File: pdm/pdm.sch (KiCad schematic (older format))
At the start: 27 parts, among them J1 Conn_01x05, J2 Conn_01x04_Male, U1 AZ1117CH-3_3TRG1, U2 SN65HVD233, U3 STM32F103C8Tx

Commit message: small changes
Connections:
- net _P: now reaches J2.3 (Pin_3), R2.2, U2.6 (CANL)
- net _N: now reaches J2.2 (Pin_2), R2.1, U2.7 (CANH)
- net PD0 renamed OSC_N
- net PD1 renamed OSC_P
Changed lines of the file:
@@
 EESchema Schematic File Version 4
+LIBS:pdm-cache
 EELAYER 30 0
 EELAYER END
@@
 	5050 4950 4850 4950
 Text Label 4850 4850 0    50   ~ 0
-PD0
+OSC_N
 Text Label 4850 4950 0    50   ~ 0
-PD1
+OSC_P
 $Comp
 L Device:C C9
@@
 	950  7350 1250 7350
 Text Label 2000 3850 2    50   ~ 0
-PD1
+OSC_P
 Wire Wire Line
 	1050 3850 1050 4550
 Text Label 2000 4550 2    50   ~ 0
-PD0
+OSC_N
 Wire Wire Line
 	1650 3850 2000 3850
@@
 	900  6850 1250 6850
 $Comp
-L power:+12V #PWR?
+L power:+12V #PWR0108
 U 1 1 5FA6CF0E
 P 1050 6500
-F 0 "#PWR?" H 1050 6350 50  0001 C CNN
+F 0 "#PWR0108" H 1050 6350 50  0001 C CNN
 F 1 "+12V" H 1065 6673 50  0000 C CNN
 F 2 "" H 1050 6500 50  0001 C CNN
@@
 	1    0    0    -1
 $EndComp
+Text Label 2850 2700 0    50   ~ 0
+_N
+Text Label 2850 2800 0    50   ~ 0
+_P
 $EndSCHEMATC

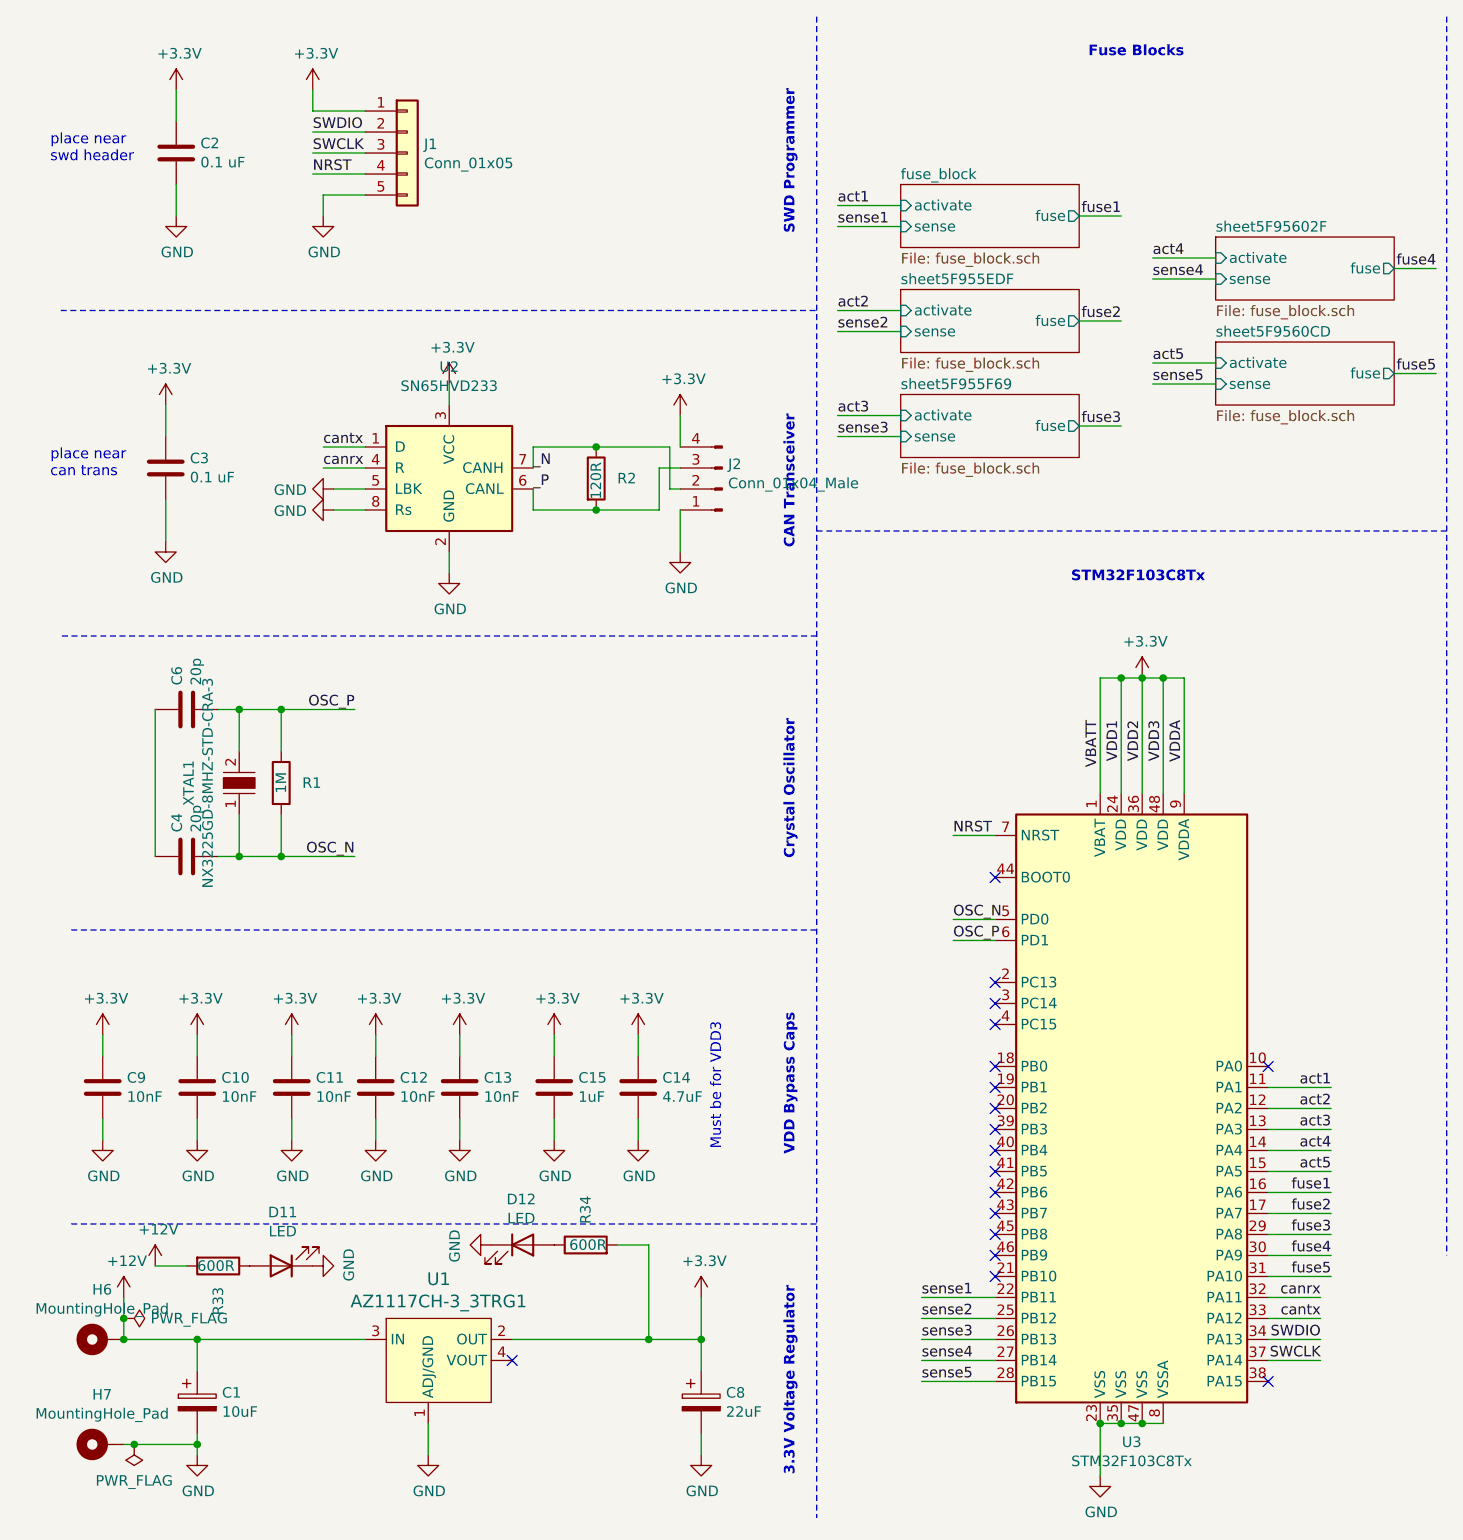
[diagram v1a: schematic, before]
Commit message: replaced with stm32f042
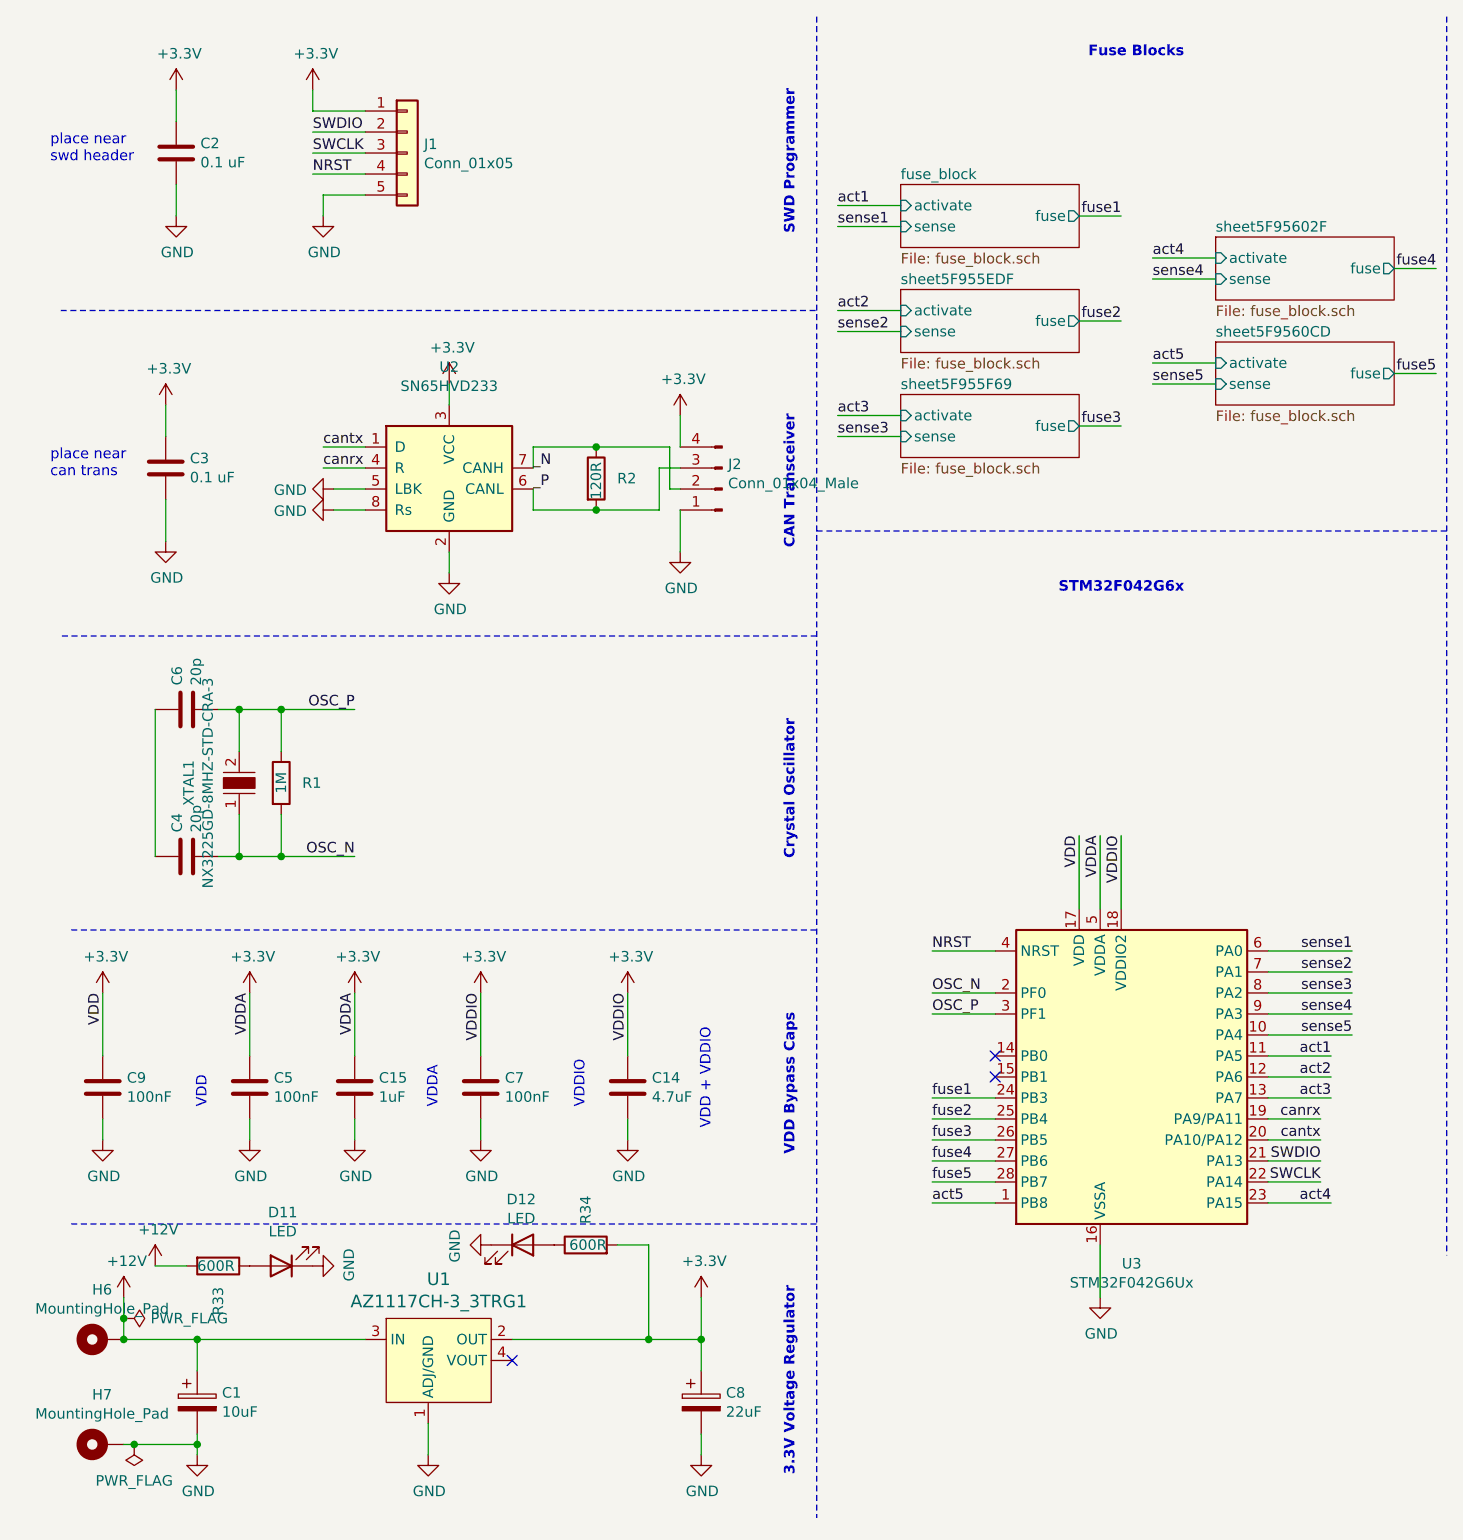
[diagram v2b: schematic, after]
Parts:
- removed C10, C11, C12, C13: 10nF, Capacitor_SMD:C_0805_2012Metric_Pad1.15x1.40mm_HandSolder, symbol Device:C
- removed U3: STM32F103C8Tx, Package_QFP:LQFP-48_7x7mm_P0.5mm, symbol MCU_ST_STM32F1:STM32F103C8Tx
- added C5, C7: 100nF, Capacitor_SMD:C_0805_2012Metric_Pad1.15x1.40mm_HandSolder, symbol Device:C
- added U3: STM32F042G6Ux, Package_DFN_QFN:QFN-28_4x4mm_P0.5mm, symbol MCU_ST_STM32F0:STM32F042G6Ux
- C9: value 10nF -> 100nF
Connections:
- net +3V3: now also C5.1, C7.1, U3.17 (VDD), U3.18 (VDDIO2), U3.5 (VDDA)
- net GND: now also C5.2, C7.2, U3.16 (VSSA)
- net NRST: now also U3.4 (NRST)
- net OSC_N: now also U3.2 (PF0)
- net OSC_P: now also U3.3 (PF1)
- net SWCLK: now also U3.22 (PA14)
- net SWDIO: now also U3.21 (PA13)
- net act1: now also U3.11 (PA5)
- net act2: now also U3.12 (PA6)
- net act3: now also U3.13 (PA7)
- net act4: now also U3.23 (PA15)
- net act5: now also U3.1 (PB8)
- net canrx: now also U3.19 (PA9/PA11)
- net cantx: now also U3.20 (PA10/PA12)
- net fuse1: now also U3.24 (PB3)
- net fuse2: now also U3.25 (PB4)
- net fuse3: now also U3.26 (PB5)
- net fuse4: now also U3.27 (PB6)
- net fuse5: now also U3.28 (PB7)
- net sense1: now also U3.6 (PA0)
- net sense2: now also U3.7 (PA1)
- net sense3: now also U3.8 (PA2)
- net sense4: now also U3.9 (PA3)
- net sense5: now also U3.10 (PA4)
- no-connect marks 18 -> 3
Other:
- note added: "STM32F042G6x"
- note added: "VDD"
- note added: "VDD + VDDIO"
- note added: "VDDA"
- note added: "VDDIO"
- note removed: "Must be for VDD3"
- note removed: "STM32F103C8Tx"
- moved on the sheet: C14, C15

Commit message: neatened up traces
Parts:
- J1: footprint Connector_PinHeader_2.00mm:PinHeader_1x06_P2.00mm_Vertical -> Connector_PinHeader_2.00mm:PinHeader_1x05_P2.00mm_Vertical
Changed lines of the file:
@@
 $EndDescr
-$Comp
-L Connector_Generic:Conn_01x05 J1
-U 1 1 5F958CF3
-P 2250 1200
-F 0 "J1" H 2330 1242 50  0000 L CNN
-F 1 "Conn_01x05" H 2330 1151 50  0000 L CNN
-F 2 "Connector_PinHeader_2.00mm:PinHeader_1x06_P2.00mm_Vertical" H 2250 1200 50  0001 C CNN
-F 3 "~" H 2250 1200 50  0001 C CNN
-	1    2250 1200
-	1    0    0    -1
-$EndComp
 $Comp
 L power:GND #PWR09
@@
 Wire Wire Line
 	2850 2900 2850 2800
-$Comp
-L dk_PMIC-Voltage-Regulators-Linear:AZ1117CH-3_3TRG1 U1
-U 1 1 5F973525
-P 2350 6850
-F 0 "U1" H 2400 7137 60  0000 C CNN
-F 1 "AZ1117CH-3_3TRG1" H 2400 7031 60  0000 C CNN
-F 2 "Package_TO_SOT_SMD:SOT-223" H 2550 7050 60  0001 L CNN
-F 3 "https://www.diodes.com/assets/Datasheets/AZ1117C.pdf" H 2550 7150 60  0001 L CNN
-F 4 "AZ1117CH-3.3TRG1DICT-ND" H 2550 7250 60  0001 L CNN "Digi-Key_PN"
-F 5 "AZ1117CH-3.3TRG1" H 2550 7350 60  0001 L CNN "MPN"
-F 6 "Integrated Circuits (ICs)" H 2550 7450 60  0001 L CNN "Category"
-F 7 "PMIC - Voltage Regulators - Linear" H 2550 7550 60  0001 L CNN "Family"
-F 8 "https://www.diodes.com/assets/Datasheets/AZ1117C.pdf" H 2550 7650 60  0001 L CNN "DK_Datasheet_Link"
-F 9 "/product-detail/en/diodes-incorporated/AZ1117CH-3.3TRG1/AZ1117CH-3.3TRG1DICT-ND/4505206" H 2550 7750 60  0001 L CNN "DK_Detail_Page"
-F 10 "IC REG LINEAR 3.3V 800MA SOT223" H 2550 7850 60  0001 L CNN "Description"
-F 11 "Diodes Incorporated" H 2550 7950 60  0001 L CNN "Manufacturer"
-F 12 "Active" H 2550 8050 60  0001 L CNN "Status"
-	1    2350 6850
-	1    0    0    -1
-$EndComp
 $Comp
 L power:+12V #PWR01
@@
 Wire Wire Line
 	900  6750 900  6850
-NoConn ~ 2750 6950
 Wire Wire Line
 	6350 6000 6600 6000
@@
 Text Label 3300 5200 3    50   ~ 0
 VDDIO
+$Comp
+L dk_PMIC-Voltage-Regulators-Linear:AZ1117CH-3_3TRG1 U1
+U 1 1 5F973525
+P 2350 6850
+F 0 "U1" H 2400 7137 60  0000 C CNN
+F 1 "AZ1117CH-3_3TRG1" H 2400 7031 60  0000 C CNN
+F 2 "Package_TO_SOT_SMD:SOT-223" H 2550 7050 60  0001 L CNN
+F 3 "https://www.diodes.com/assets/Datasheets/AZ1117C.pdf" H 2550 7150 60  0001 L CNN
+F 4 "AZ1117CH-3.3TRG1DICT-ND" H 2550 7250 60  0001 L CNN "Digi-Key_PN"
+F 5 "AZ1117CH-3.3TRG1" H 2550 7350 60  0001 L CNN "MPN"
+F 6 "Integrated Circuits (ICs)" H 2550 7450 60  0001 L CNN "Category"
+F 7 "PMIC - Voltage Regulators - Linear" H 2550 7550 60  0001 L CNN "Family"
+F 8 "https://www.diodes.com/assets/Datasheets/AZ1117C.pdf" H 2550 7650 60  0001 L CNN "DK_Datasheet_Link"
+F 9 "/product-detail/en/diodes-incorporated/AZ1117CH-3.3TRG1/AZ1117CH-3.3TRG1DICT-ND/4505206" H 2550 7750 60  0001 L CNN "DK_Detail_Page"
+F 10 "IC REG LINEAR 3.3V 800MA SOT223" H 2550 7850 60  0001 L CNN "Description"
+F 11 "Diodes Incorporated" H 2550 7950 60  0001 L CNN "Manufacturer"
+F 12 "Active" H 2550 8050 60  0001 L CNN "Status"
+	1    2350 6850
+	1    0    0    -1
+$EndComp
+$Comp
+L Connector_Generic:Conn_01x05 J1
+U 1 1 5F958CF3
+P 2250 1200
+F 0 "J1" H 2330 1242 50  0000 L CNN
+F 1 "Conn_01x05" H 2330 1151 50  0000 L CNN
+F 2 "Connector_PinHeader_2.00mm:PinHeader_1x05_P2.00mm_Vertical" H 2250 1200 50  0001 C CNN
+F 3 "~" H 2250 1200 50  0001 C CNN
+	1    2250 1200
+	1    0    0    -1
+$EndComp
+NoConn ~ 2750 6950
 $EndSCHEMATC
